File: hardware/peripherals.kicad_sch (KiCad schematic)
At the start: 26 parts, among them J6 Conn_01x02, J7 Conn_01x03, J8 USB_C_Receptacle_USB2.0_14P, SW1 SW_Push, U3 74AHCT1G125, U4 USBLC6-2SC6, U5 DS3231MZ

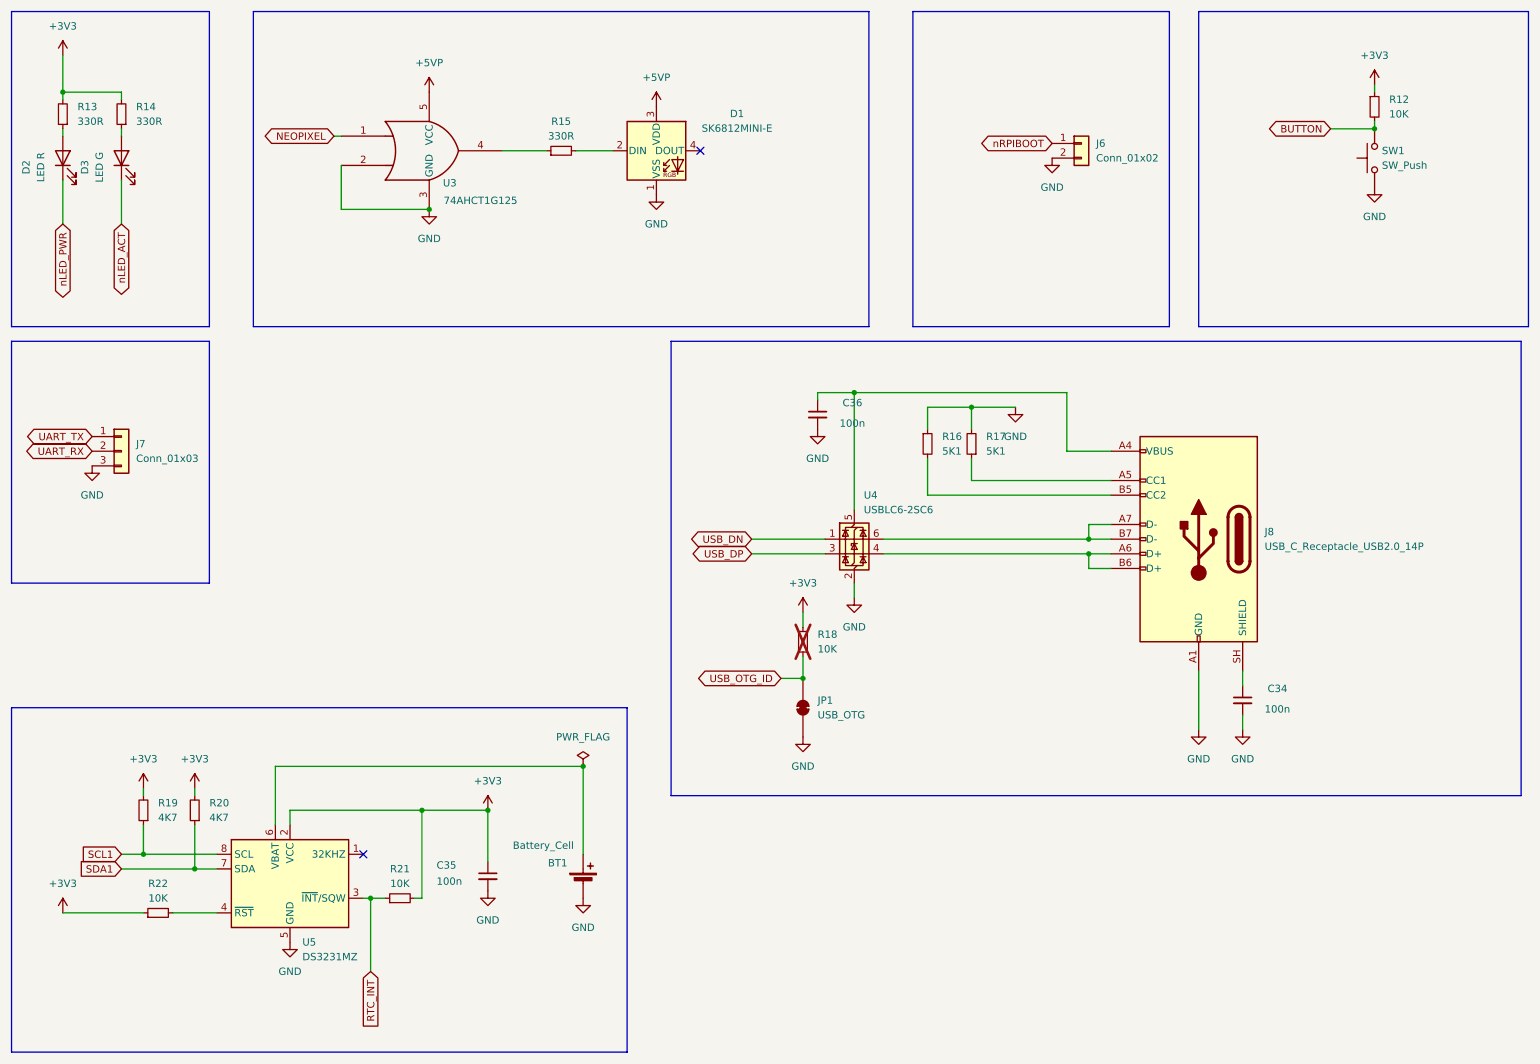
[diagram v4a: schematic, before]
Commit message: Add hardware wake circuit: 2N7002 + 74AHCT1G32 OR gate
RTC alarm → N-FET inverter → OR gate → GLOBAL_EN
GPIO6 (GPIO_HOLD) keeps CM4 alive after boot.
All wake components DNP for v1 (pull-up fallback).
v2: populate wake circuit, remove GLOBAL_EN pull-up.
ERC: 0 errors, 0 warnings
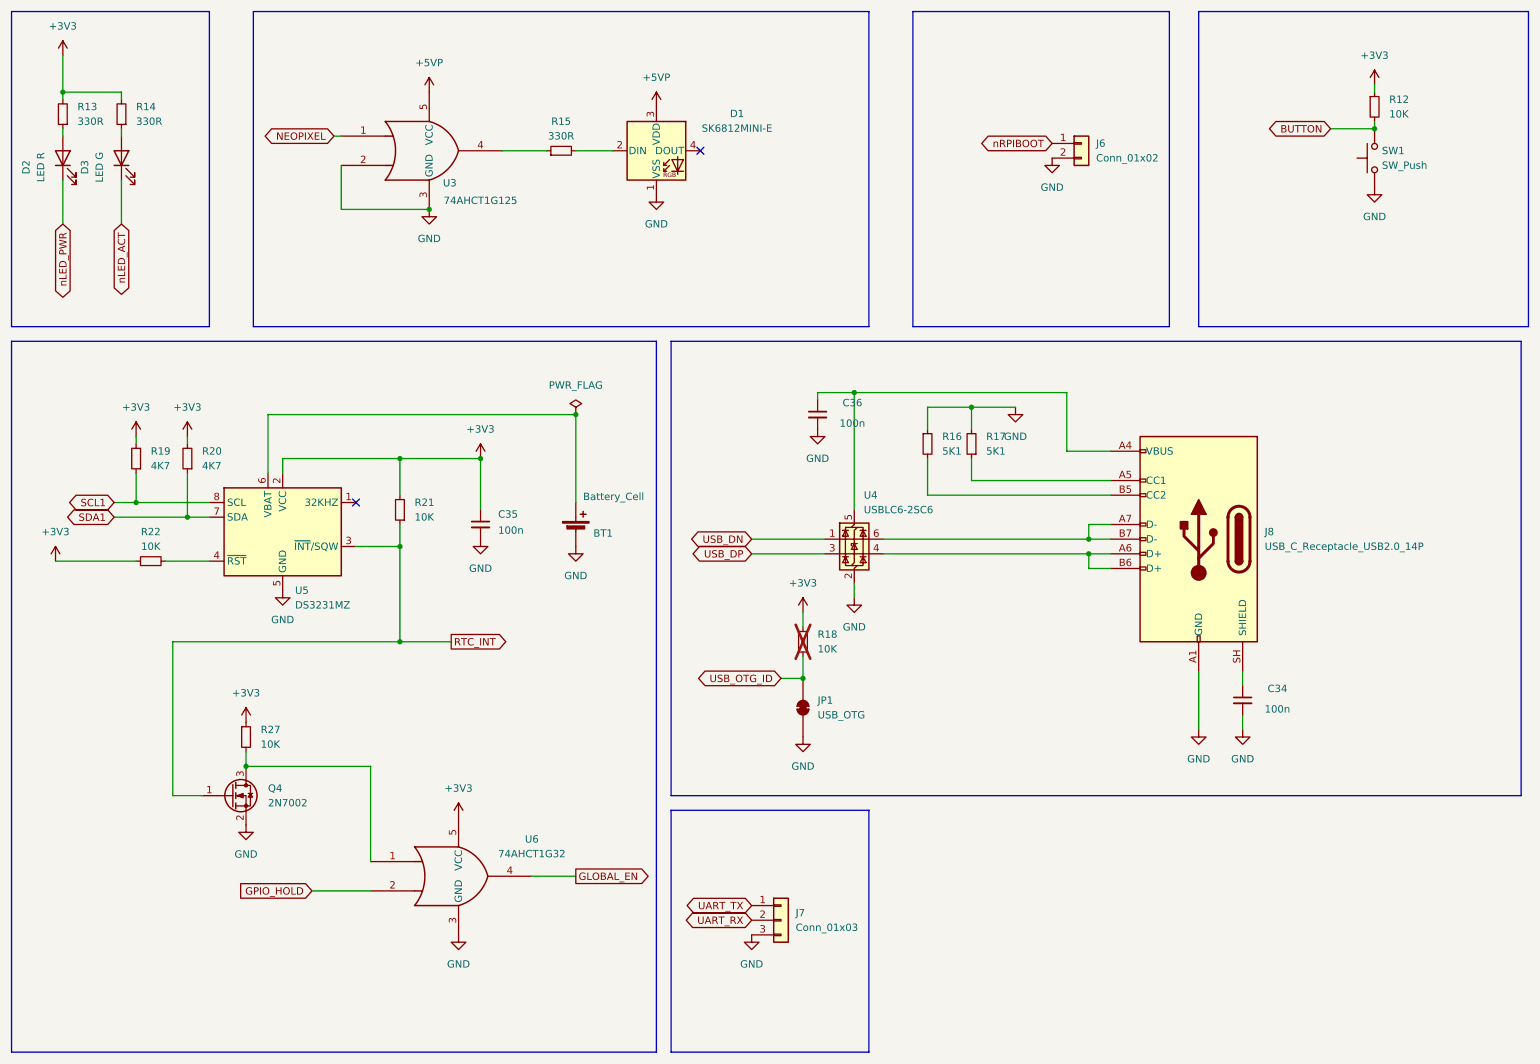
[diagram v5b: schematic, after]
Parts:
- added Q4: 2N7002, Package_TO_SOT_SMD:SOT-23, symbol Transistor_FET:2N7002
- added R27: 10K, Resistor_SMD:R_0805_2012Metric, symbol Device:R_Small
- added U6: 74AHCT1G32, symbol 74xGxx:74AHCT1G32
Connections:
- net +3V3: now also R27.1, U6.5 (VCC)
- net GND: now also Q4.2 (S), U6.3 (GND)
- net RTC_INT: now also Q4.1 (G)
- new net: Q4.3 (D), R27.2, U6.1
- new net GLOBAL_EN: U6.4
- new net GPIO_HOLD: U6.2
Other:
- moved on the sheet: BT1, C35, J7, R19, R20, R21, R22, U5

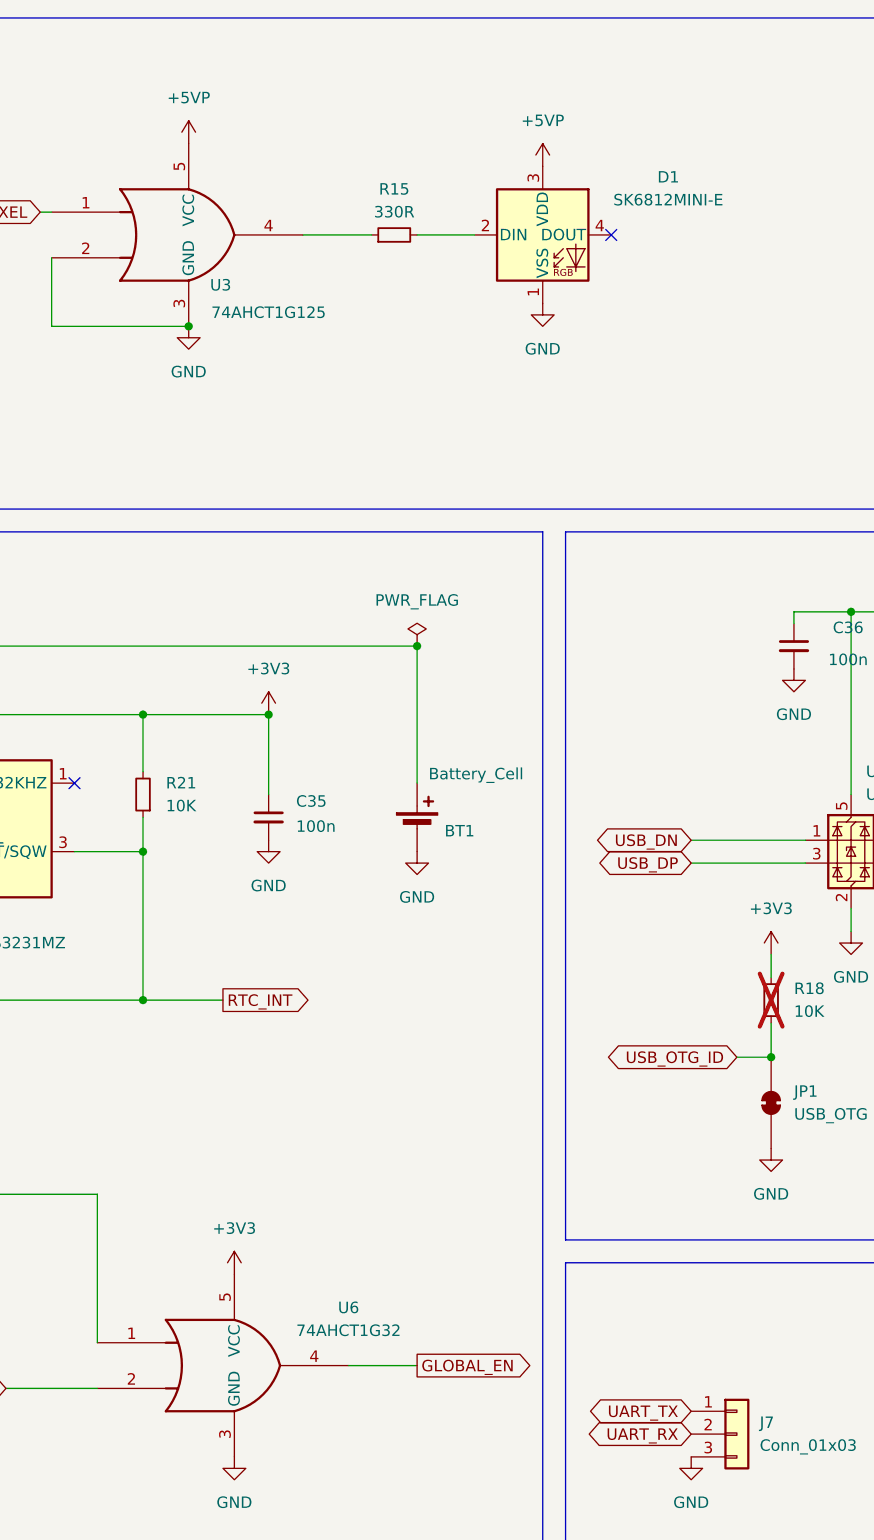
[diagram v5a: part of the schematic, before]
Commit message: Add missing decoupling caps: wake OR gate, NeoPixel OR gate, SK6812
- C37: 100nF on U3 (NeoPixel OR gate, 5V)
- C38: 100nF on D1 (SK6812MINI-E VDD, 5V)
- C39: 100nF on U6 (wake OR gate, 3.3V)
- ERC: 0 errors, 0 warnings
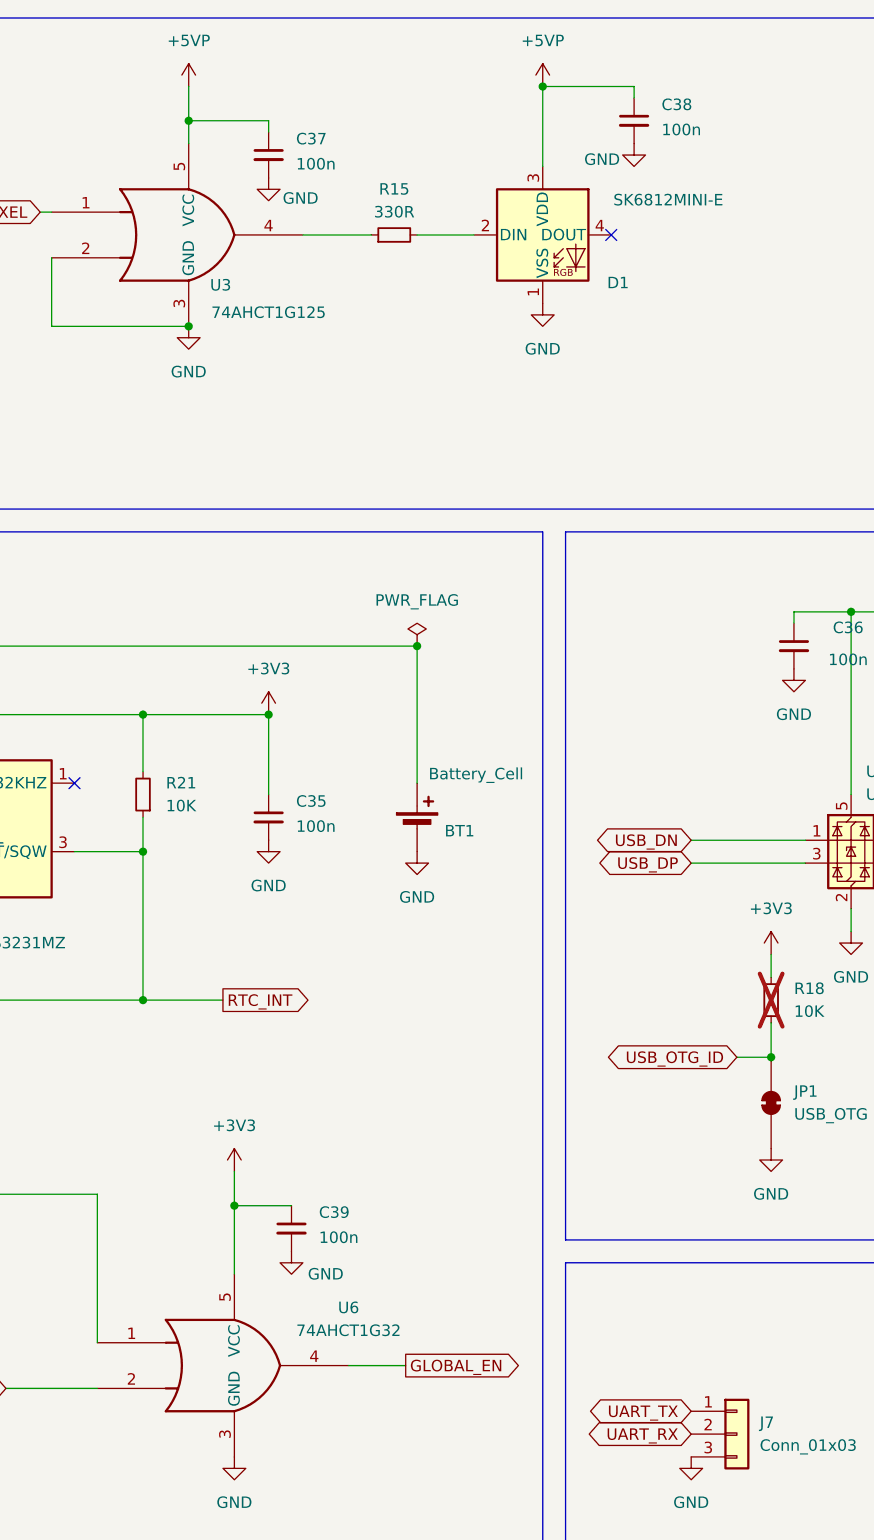
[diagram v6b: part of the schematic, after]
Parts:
- added C37, C38, C39: 100n, Capacitor_SMD:C_0805_2012Metric, symbol Device:C_Small
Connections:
- net +3V3: now also C39.1
- net +5VP: now also C37.1, C38.1
- net GND: now also C37.2, C38.2, C39.2

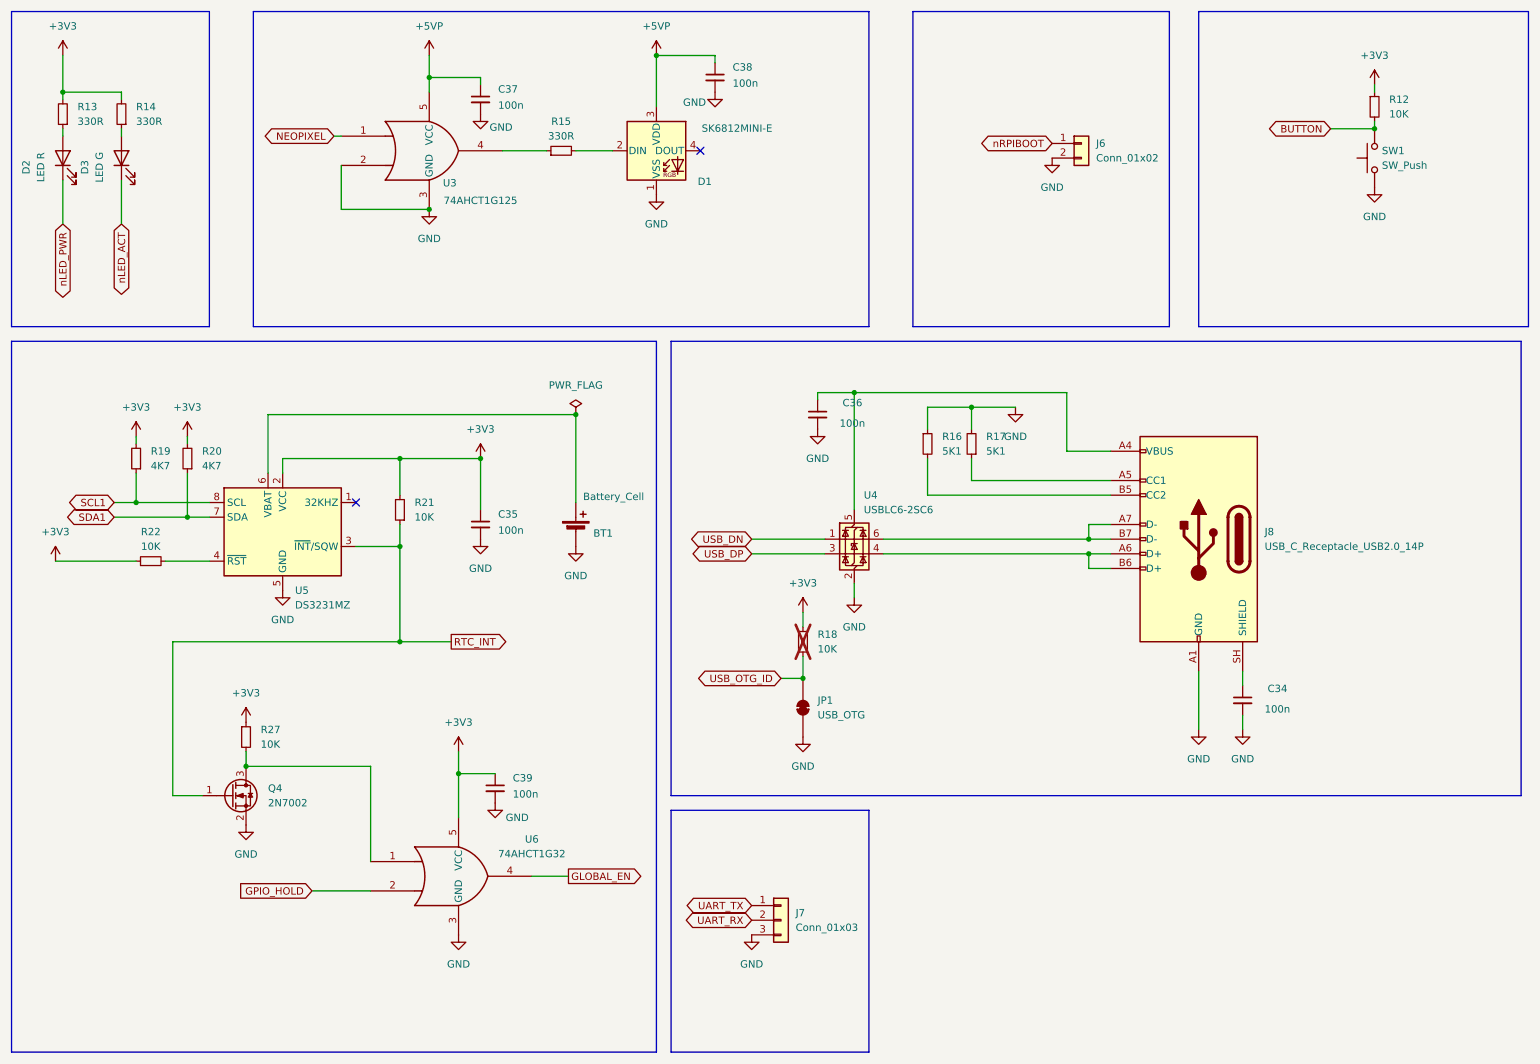
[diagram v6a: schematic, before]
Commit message: Re-annotate all components
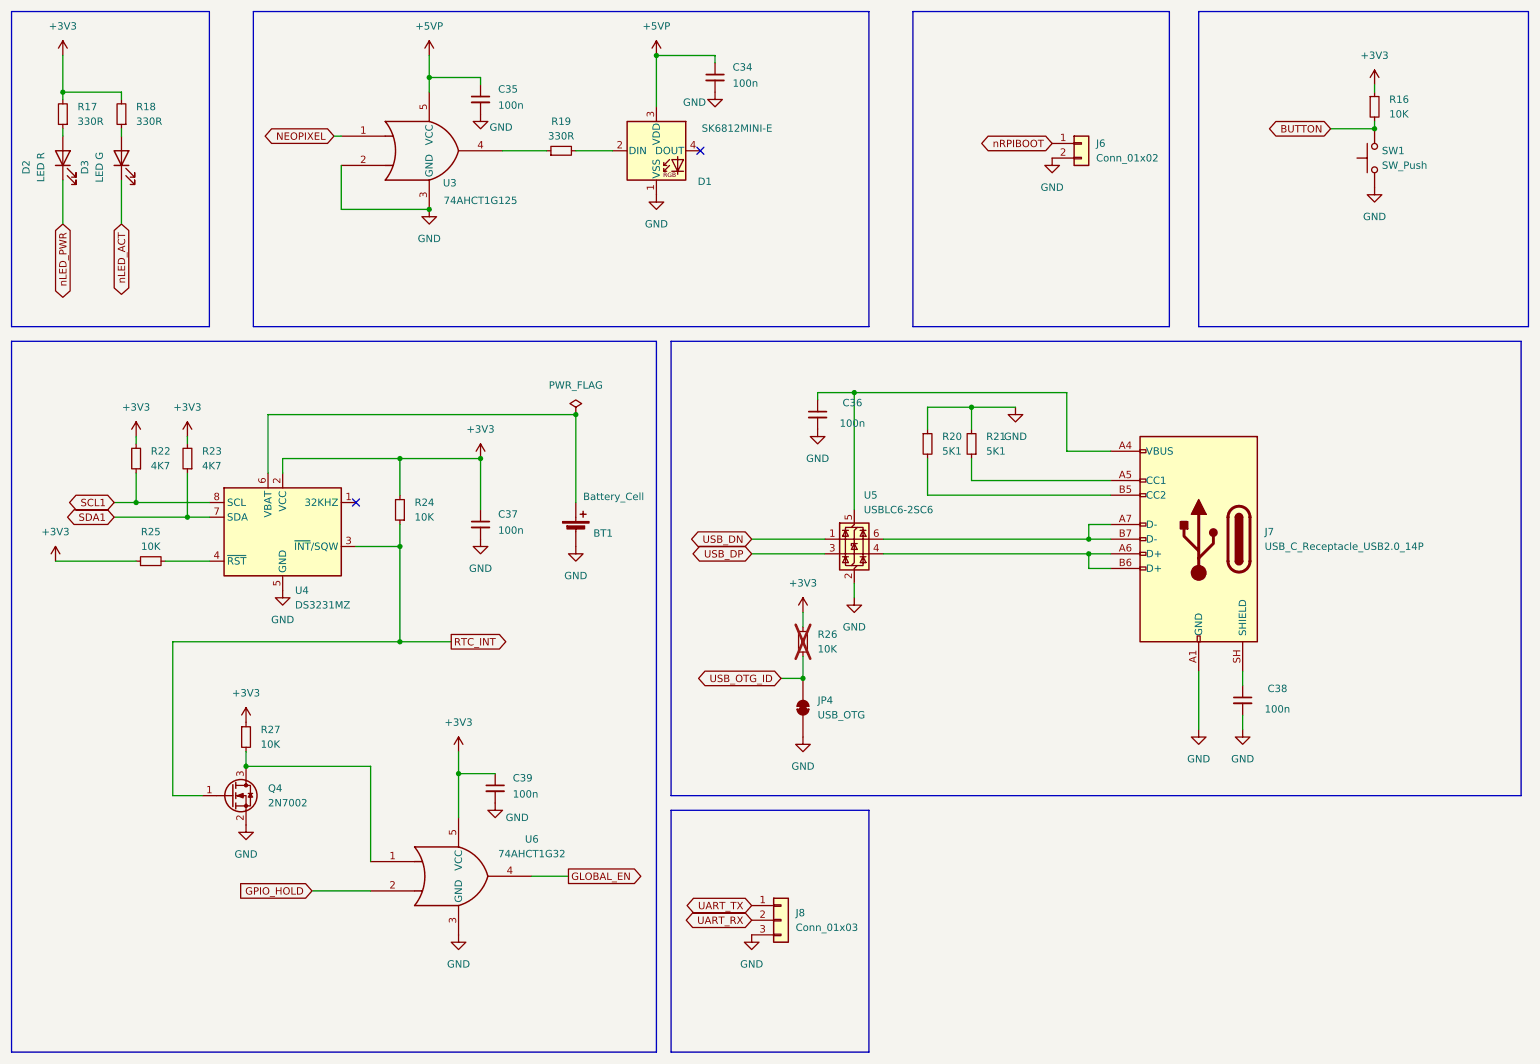
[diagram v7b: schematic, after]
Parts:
- renumbered C38 to C34, C37 to C35, C35 to C37, C34 to C38, J8 to J7, J7 to J8, JP1 to JP4, R12 to R16, R13 to R17, R14 to R18, R15 to R19, R16 to R20, R17 to R21, R19 to R22, R20 to R23, R21 to R24, R22 to R25, R18 to R26, U5 to U4, U4 to U5

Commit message: Assign missing footprints: R12-R15 (0805), JP1-JP3 (solder jumper), U6 (SOT-23-5)
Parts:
- U6: footprint (none) -> Package_TO_SOT_SMD:SOT-23-5
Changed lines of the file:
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@@
 			)
 		)
-		(property "Footprint" ""
+		(property "Footprint" "Package_TO_SOT_SMD:SOT-23-5"
 			(at 92.71 165.1 0)
 			(hide yes)
